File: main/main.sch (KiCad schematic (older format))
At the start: 2 parts, among them J2 AudioJack3, J3 Conn_02x10_Odd_Even

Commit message: Some cleanup
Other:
- note added: "Analog Output (TODO)"
- note added: "The debug interface uses the SW-DP protocol. This is a packet \nbased protocol that uses a unidirectional clock signal (DBG_SWCLK) \nand a bi-directional data signal (DBG_SWDIO). The debugger (usually)\ndrives the clock signal, while the data-line can be driven be either two.\nThe DBG_SWO line is optionally included for debug output.\n\nhttps://www.silabs.com/documents/public/application-notes/AN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"
- note removed: "Analog Output"
- note removed: "The debug interface uses the SW-DP protocol. This is a packet based protocol\nthat uses a unidirectional clock signal (DBG_SWCLK) and a bi-directional data\nsignal (DBG_SWDIO). The debugger (usually) drives the clock signal, while\nthe data-line can be driven be either two. The DBG_SWO line is optionally\nincluded for debug output.\n\nhttps://www.silabs.com/documents/public/application-notes/AN00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"
- moved on the sheet: J2, J3
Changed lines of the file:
@@
 $Descr A4 11693 8268
 encoding utf-8
-Sheet 1 4
+Sheet 1 3
 Title "Synthesizer"
 Date "2021-09-06"
@@
 L Connector:AudioJack3 J2
 U 1 1 61366BDF
-P 3000 4700
-F 0 "J2" H 2720 4633 50  0000 R CNN
-F 1 "AudioJack3" H 2720 4724 50  0000 R CNN
-F 2 "" H 3000 4700 50  0001 C CNN
-F 3 "~" H 3000 4700 50  0001 C CNN
-	1    3000 4700
+P 1300 7150
+F 0 "J2" H 1020 7083 50  0000 R CNN
+F 1 "AudioJack3" H 1020 7174 50  0000 R CNN
+F 2 "" H 1300 7150 50  0001 C CNN
+F 3 "~" H 1300 7150 50  0001 C CNN
+	1    1300 7150
 	-1   0    0    1
 $EndComp
@@
 L power:GND #PWR0101
 U 1 1 61367C82
-P 2700 4950
-F 0 "#PWR0101" H 2700 4700 50  0001 C CNN
-F 1 "GND" H 2705 4777 50  0000 C CNN
-F 2 "" H 2700 4950 50  0001 C CNN
-F 3 "" H 2700 4950 50  0001 C CNN
-	1    2700 4950
+P 1000 7400
+F 0 "#PWR0101" H 1000 7150 50  0001 C CNN
+F 1 "GND" H 1005 7227 50  0000 C CNN
+F 2 "" H 1000 7400 50  0001 C CNN
+F 3 "" H 1000 7400 50  0001 C CNN
+	1    1000 7400
 	1    0    0    -1
 $EndComp
 Wire Wire Line
-	2700 4950 2700 4800
+	1000 7400 1000 7250
 Wire Wire Line
-	2700 4800 2800 4800
-Text GLabel 2800 4600 0    50   Input ~ 0
+	1000 7250 1100 7250
+Text GLabel 1100 7050 0    50   Input ~ 0
 DAC0
-Text GLabel 2800 4700 0    50   Input ~ 0
+Text GLabel 1100 7150 0    50   Input ~ 0
 DAC1
 Wire Notes Line
-	550  3450 4250 3450
+	550  6700 2150 6700
 Wire Notes Line
-	4250 5250 550  5250
-Text Notes 600  3600 0    50   ~ 10
-Analog Output
+	2150 7700 550  7700
+Text Notes 600  6850 0    50   ~ 10
+Analog Output (TODO)
 Wire Notes Line
-	4250 3450 4250 5250
+	2150 6700 2150 7700
 Wire Notes Line
-	550  5250 550  3450
+	550  7700 550  6700
 Wire Notes Line
-	7450 2900 11150 2900
-Wire Notes Line
-	11150 2900 11150 550
-Wire Notes Line
-	11150 550  7450 550
-Wire Notes Line
-	7450 550  7450 2900
-Text Notes 7500 650  0    50   ~ 10
-EFM32 Debug Interface
+	11150 550  7200 550
+$Sheet
+S 4800 2250 1900 1550
+U 6139E7E0
+F0 "MCU" 50
+F1 "MCU.sch" 50
+F2 "DBG_SWDIO" O R 6700 3100 50
+F3 "DBG_SWCLK" O R 6700 3200 50
+F4 "DBG_SWO" O R 6700 3400 50
+F5 "RESETn" O R 6700 3500 50
+F6 "VMCU" O R 6700 2800 50
+F7 "UO_RX_#1" I L 4800 2400 50
+$EndSheet
+$Sheet
+S 3450 700  700  250
+U 613F97F2
+F0 "MIDI-IN" 50
+F1 "MIDI-IN.sch" 50
+F2 "MIDI_IN" O R 4150 850 50
+$EndSheet
+Text Notes 8250 1500 0    50   Italic 0
+The debug interface uses the SW-DP protocol. This is a packet \nbased protocol that uses a unidirectional clock signal (DBG_SWCLK) \nand a bi-directional data signal (DBG_SWDIO). The debugger (usually)\ndrives the clock signal, while the data-line can be driven be either two.\nThe DBG_SWO line is optionally included for debug output.\n\nhttps://www.silabs.com/documents/public/application-notes/AN0043.pdf
+NoConn ~ 7400 1800
+NoConn ~ 7400 1700
+Wire Wire Line
+	8100 1100 8100 1200
+Connection ~ 8100 1100
+Wire Wire Line
+	8100 1000 8100 1100
+Wire Wire Line
+	7900 1000 8100 1000
+Connection ~ 8100 1200
+Wire Wire Line
+	7900 1100 8100 1100
+Wire Wire Line
+	8100 1300 8100 1400
+Connection ~ 8100 1300
+Wire Wire Line
+	8100 1200 8100 1300
+Wire Wire Line
+	7900 1200 8100 1200
+Connection ~ 8100 1400
+Wire Wire Line
+	7900 1300 8100 1300
+Wire Wire Line
+	8100 1500 8100 1600
+Connection ~ 8100 1500
+Wire Wire Line
+	8100 1400 8100 1500
+Wire Wire Line
+	7900 1400 8100 1400
+Wire Wire Line
+	8100 1600 8100 1700
+Connection ~ 8100 1600
+Wire Wire Line
+	7900 1500 8100 1500
+Connection ~ 8100 1700
+Wire Wire Line
+	7900 1600 8100 1600
+Wire Wire Line
+	8100 1800 8100 1850
+Connection ~ 8100 1800
+Wire Wire Line
+	8100 1700 8100 1800
+Wire Wire Line
+	7900 1700 8100 1700
+Wire Wire Line
+	7900 1800 8100 1800
+$Comp
+L power:GND #PWR04
+U 1 1 613B8CA5
+P 8100 1850
+F 0 "#PWR04" H 8100 1600 50  0001 C CNN
+F 1 "GND" H 8105 1677 50  0000 C CNN
+F 2 "" H 8100 1850 50  0001 C CNN
+F 3 "" H 8100 1850 50  0001 C CNN
+	1    8100 1850
+	1    0    0    -1
+$EndComp
+NoConn ~ 7400 1400
+NoConn ~ 7400 1100
+NoConn ~ 7400 1000
+NoConn ~ 7900 900
 $Comp
 L Connector_Generic:Conn_02x10_Odd_Even J3
 U 1 1 613A6A76
-P 9750 2050
-F 0 "J3" H 9800 2667 50  0000 C CNN
-F 1 "Conn_02x10_Odd_Even" H 9800 2576 50  0000 C CNN
-F 2 "" H 9750 2050 50  0001 C CNN
-F 3 "~" H 9750 2050 50  0001 C CNN
-	1    9750 2050
+P 7600 1300
+F 0 "J3" H 7650 1917 50  0000 C CNN
+F 1 "Conn_02x10_Odd_Even" H 7650 1826 50  0000 C CNN
+F 2 "" H 7600 1300 50  0001 C CNN
+F 3 "~" H 7600 1300 50  0001 C CNN
+	1    7600 1300
 	1    0    0    -1
 $EndComp
-NoConn ~ 10050 1650
-NoConn ~ 9550 1750
-NoConn ~ 9550 1850
-NoConn ~ 9550 2150
-$Comp
-L power:GND #PWR04
-U 1 1 613B8CA5
-P 10200 2600
-F 0 "#PWR04" H 10200 2350 50  0001 C CNN
-F 1 "GND" H 10205 2427 50  0000 C CNN
-F 2 "" H 10200 2600 50  0001 C CNN
-F 3 "" H 10200 2600 50  0001 C CNN
-	1    10200 2600
-	1    0    0    -1
-$EndComp
+Text Notes 8250 800  0    50   ~ 10
+EFM32 Debug Interface
+Wire Notes Line
+	7200 550  7200 2150
+Wire Notes Line
+	11150 2150 11150 550
+Wire Notes Line
+	7200 2150 11150 2150
 Wire Wire Line
-	10050 2550 10200 2550
+	6700 2800 6950 2800
 Wire Wire Line
-	10050 2450 10200 2450
+	6950 2800 6950 900
 Wire Wire Line
-	10200 2450 10200 2550
-Connection ~ 10200 2550
+	6950 900  7400 900
 Wire Wire Line
-	10200 2550 10200 2600
+	6700 3100 7000 3100
 Wire Wire Line
-	10050 2350 10200 2350
-Connection ~ 10200 2450
+	7000 3100 7000 1200
 Wire Wire Line
-	10050 2250 10200 2250
-Connection ~ 10200 2350
+	7000 1200 7400 1200
 Wire Wire Line
-	10200 2350 10200 2450
+	6700 3200 7050 3200
 Wire Wire Line
-	10050 2150 10200 2150
+	7050 3200 7050 1300
 Wire Wire Line
-	10200 2150 10200 2250
-Connection ~ 10200 2250
+	7050 1300 7400 1300
 Wire Wire Line
-	10200 2250 10200 2350
+	6700 3400 7100 3400
 Wire Wire Line
-	10050 2050 10200 2050
-Connection ~ 10200 2150
+	7100 3400 7100 1500
 Wire Wire Line
-	10050 1950 10200 1950
+	7100 1500 7400 1500
 Wire Wire Line
-	10200 1950 10200 2050
-Connection ~ 10200 2050
+	6700 3500 7150 3500
 Wire Wire Line
-	10200 2050 10200 2150
+	7150 3500 7150 1600
 Wire Wire Line
-	10050 1850 10200 1850
-Connection ~ 10200 1950
+	7150 1600 7400 1600
 Wire Wire Line
-	10050 1750 10200 1750
+	4150 850  4500 850
 Wire Wire Line
-	10200 1750 10200 1850
-Connection ~ 10200 1850
+	4500 850  4500 2400
 Wire Wire Line
-	10200 1850 10200 1950
-NoConn ~ 9550 2450
-NoConn ~ 9550 2550
-Text Notes 7500 1250 0    50   Italic 0
-The debug interface uses the SW-DP protocol. This is a packet based protocol\nthat uses a unidirectional clock signal (DBG_SWCLK) and a bi-directional data\nsignal (DBG_SWDIO). The debugger (usually) drives the clock signal, while\nthe data-line can be driven be either two. The DBG_SWO line is optionally\nincluded for debug output.\n\nhttps://www.silabs.com/documents/public/application-notes/AN0043.pdf
-$Sheet
-S 4950 2950 1900 1700
-U 6139EB2D
-F0 "FPGA" 50
-F1 "FPGA.sch" 50
-$EndSheet
-Wire Wire Line
-	9550 2350 8000 2350
-Wire Wire Line
-	8000 2350 8000 2000
-Wire Wire Line
-	8000 2000 6850 2000
-Wire Wire Line
-	9550 2250 8100 2250
-Wire Wire Line
-	8100 2250 8100 1900
-Wire Wire Line
-	8100 1900 6850 1900
-Wire Wire Line
-	9550 2050 8200 2050
-Wire Wire Line
-	8200 2050 8200 1750
-Wire Wire Line
-	8200 1750 6850 1750
-Wire Wire Line
-	9550 1950 8300 1950
-Wire Wire Line
-	8300 1950 8300 1650
-Wire Wire Line
-	8300 1650 6850 1650
-Wire Wire Line
-	9550 1650 8400 1650
-Wire Wire Line
-	8400 1650 8400 1500
-Wire Wire Line
-	8400 1500 6850 1500
-$Sheet
-S 4950 1100 1900 1550
-U 6139E7E0
-F0 "MCU" 50
-F1 "MCU.sch" 50
-F2 "DBG_SWDIO" O R 6850 1650 50
-F3 "DBG_SWCLK" O R 6850 1750 50
-F4 "DBG_SWO" O R 6850 1900 50
-F5 "RESETn" O R 6850 2000 50
-F6 "VMCU" O R 6850 1500 50
-F7 "UO_RX_#1" O L 4950 2550 50
-$EndSheet
-$Sheet
-S 850  1150 700  250
-U 613F97F2
-F0 "MIDI-IN" 50
-F1 "MIDI-IN.sch" 50
-F2 "MIDI_IN" O R 1550 1300 50
-$EndSheet
-Wire Wire Line
-	1550 1300 3200 1300
-Wire Wire Line
-	3200 1300 3200 2550
-Wire Wire Line
-	3200 2550 4950 2550
+	4500 2400 4800 2400
 $EndSCHEMATC

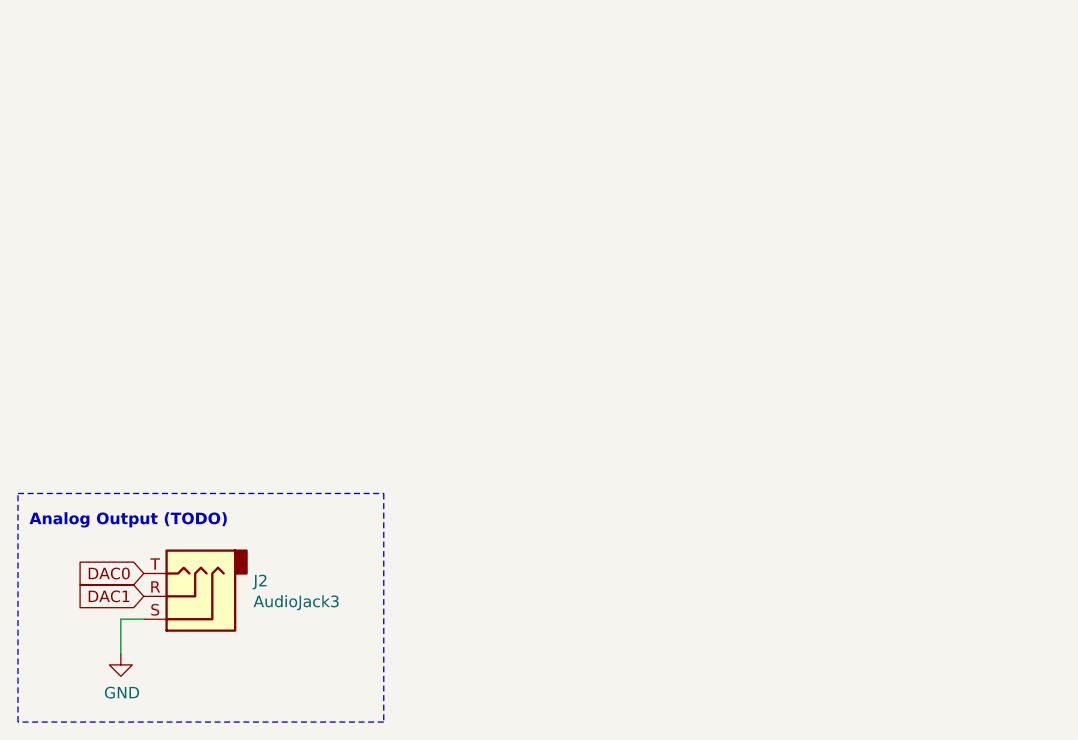
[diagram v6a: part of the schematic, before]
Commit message: Add PCM1780DBQ footprint
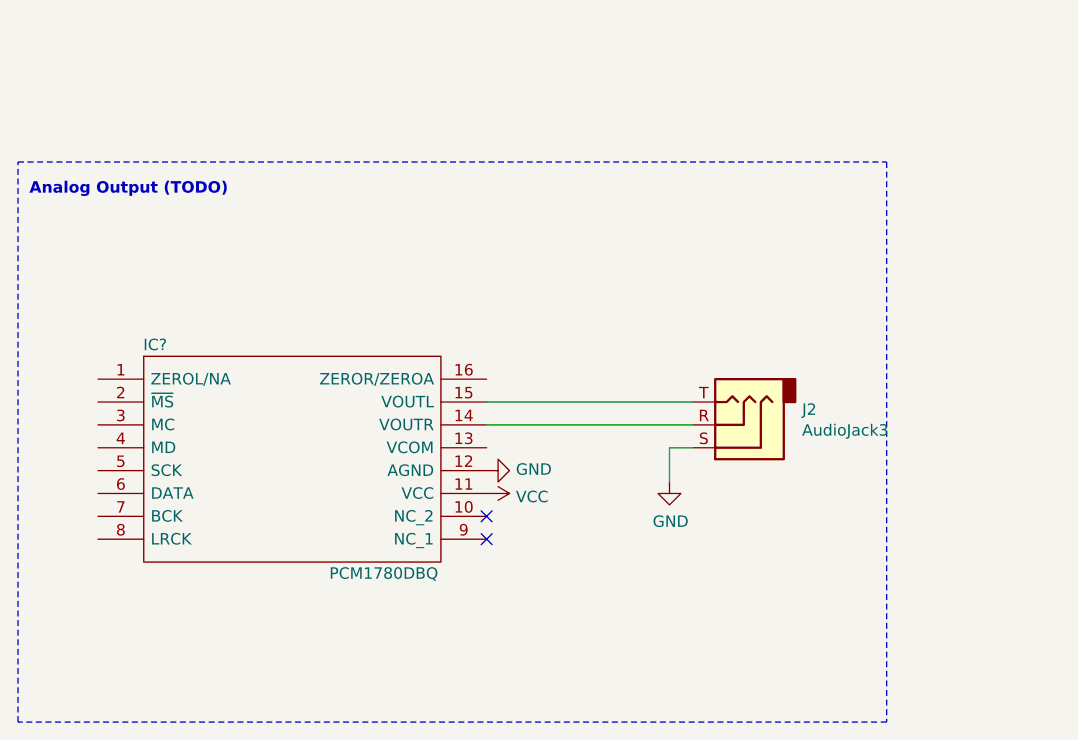
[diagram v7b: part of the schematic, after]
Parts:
- added IC?: PCM1780DBQ, SOP64P600X175-16N, symbol PCM1780DBQ:PCM1780DBQ
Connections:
- net GND: now also IC?.12 (AGND)
- net DAC0: no longer names the net of J2.T
- net DAC0: now also IC?.15 (VOUTL)
- net DAC1: no longer names the net of J2.R
- net DAC1: now also IC?.14 (VOUTR)
- new net VCC: IC?.11 (VCC)
- no-connect marks 6 -> 8
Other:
- moved on the sheet: J2
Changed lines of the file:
@@
 L Connector:AudioJack3 J2
 U 1 1 61366BDF
-P 1300 7150
-F 0 "J2" H 1020 7083 50  0000 R CNN
-F 1 "AudioJack3" H 1020 7174 50  0000 R CNN
-F 2 "" H 1300 7150 50  0001 C CNN
-F 3 "~" H 1300 7150 50  0001 C CNN
-	1    1300 7150
+P 3700 6400
+F 0 "J2" H 3420 6333 50  0000 R CNN
+F 1 "AudioJack3" H 3420 6424 50  0000 R CNN
+F 2 "" H 3700 6400 50  0001 C CNN
+F 3 "~" H 3700 6400 50  0001 C CNN
+	1    3700 6400
 	-1   0    0    1
 $EndComp
@@
 L power:GND #PWR0101
 U 1 1 61367C82
-P 1000 7400
-F 0 "#PWR0101" H 1000 7150 50  0001 C CNN
-F 1 "GND" H 1005 7227 50  0000 C CNN
-F 2 "" H 1000 7400 50  0001 C CNN
-F 3 "" H 1000 7400 50  0001 C CNN
-	1    1000 7400
-	1    0    0    -1
-$EndComp
-Wire Wire Line
-	1000 7400 1000 7250
-Wire Wire Line
-	1000 7250 1100 7250
-Text GLabel 1100 7050 0    50   Input ~ 0
-DAC0
-Text GLabel 1100 7150 0    50   Input ~ 0
-DAC1
-Wire Notes Line
-	550  6700 2150 6700
-Wire Notes Line
-	2150 7700 550  7700
-Text Notes 600  6850 0    50   ~ 10
+P 3400 6650
+F 0 "#PWR0101" H 3400 6400 50  0001 C CNN
+F 1 "GND" H 3405 6477 50  0000 C CNN
+F 2 "" H 3400 6650 50  0001 C CNN
+F 3 "" H 3400 6650 50  0001 C CNN
+	1    3400 6650
+	1    0    0    -1
+$EndComp
+Wire Wire Line
+	3400 6650 3400 6500
+Wire Wire Line
+	3400 6500 3500 6500
+Wire Notes Line
+	550  5250 4350 5250
+Wire Notes Line
+	4350 7700 550  7700
+Text Notes 600  5400 0    50   ~ 10
 Analog Output (TODO)
 Wire Notes Line
-	2150 6700 2150 7700
-Wire Notes Line
-	550  7700 550  6700
+	550  7700 550  5250
 Wire Notes Line
 	11150 550  7200 550
@@
 Wire Wire Line
 	4500 2400 4800 2400
+$Comp
+L power:VCC #PWR?
+U 1 1 613A81F9
+P 2600 6700
+F 0 "#PWR?" H 2600 6550 50  0001 C CNN
+F 1 "VCC" V 2615 6828 50  0000 L CNN
+F 2 "" H 2600 6700 50  0001 C CNN
+F 3 "" H 2600 6700 50  0001 C CNN
+	1    2600 6700
+	0    1    1    0
+$EndComp
+NoConn ~ 2600 6900
+NoConn ~ 2600 6800
+$Comp
+L PCM1780DBQ:PCM1780DBQ IC?
+U 1 1 613A1DD6
+P 900 6200
+F 0 "IC?" H 1150 6350 50  0000 C CNN
+F 1 "PCM1780DBQ" H 2150 5350 50  0000 C CNN
+F 2 "SOP64P600X175-16N" H 2450 6300 50  0001 L CNN
+F 3 "http://www.ti.com/lit/gpn/pcm1780" H 2450 6200 50  0001 L CNN
+F 4 "PCM1780DBQ, Audio DAC Octal 24 bit-, 192ksps Serial, 16-Pin SSOP" H 2450 6100 50  0001 L CNN "Description"
+F 5 "1.75" H 2450 6000 50  0001 L CNN "Height"
+F 6 "Texas Instruments" H 2450 5900 50  0001 L CNN "Manufacturer_Name"
+F 7 "PCM1780DBQ" H 2450 5800 50  0001 L CNN "Manufacturer_Part_Number"
+F 8 "595-PCM1780DBQ" H 2450 5700 50  0001 L CNN "Mouser Part Number"
+F 9 "https://www.mouser.co.uk/ProductDetail/Texas-Instruments/PCM1780DBQ?qs=wgAEGBTxy7ndC3AC4ryJQw%3D%3D" H 2450 5600 50  0001 L CNN "Mouser Price/Stock"
+F 10 "PCM1780DBQ" H 2450 5500 50  0001 L CNN "Arrow Part Number"
+F 11 "https://www.arrow.com/en/products/pcm1780dbq/texas-instruments?region=nac" H 2450 5400 50  0001 L CNN "Arrow Price/Stock"
+	1    900  6200
+	1    0    0    -1
+$EndComp
+Wire Notes Line
+	4350 5250 4350 7700
+Wire Wire Line
+	2600 6400 3500 6400
+Wire Wire Line
+	2600 6300 3500 6300
+$Comp
+L power:GND #PWR?
+U 1 1 613B4268
+P 2600 6600
+F 0 "#PWR?" H 2600 6350 50  0001 C CNN
+F 1 "GND" V 2605 6472 50  0000 R CNN
+F 2 "" H 2600 6600 50  0001 C CNN
+F 3 "" H 2600 6600 50  0001 C CNN
+	1    2600 6600
+	0    -1   -1   0
+$EndComp
 $EndSCHEMATC
